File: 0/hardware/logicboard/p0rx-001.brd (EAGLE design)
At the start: 91 x 57 mm, 37 parts, among them IC1 LTC485N, IC2 LTC485N, IC3 LTC485N, IC4 LTC485N, IC5 74ALS05N, IC6 74ALS05N, J0 DC5V, J10 DIN5, J7 DIN5, J8 DIN5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

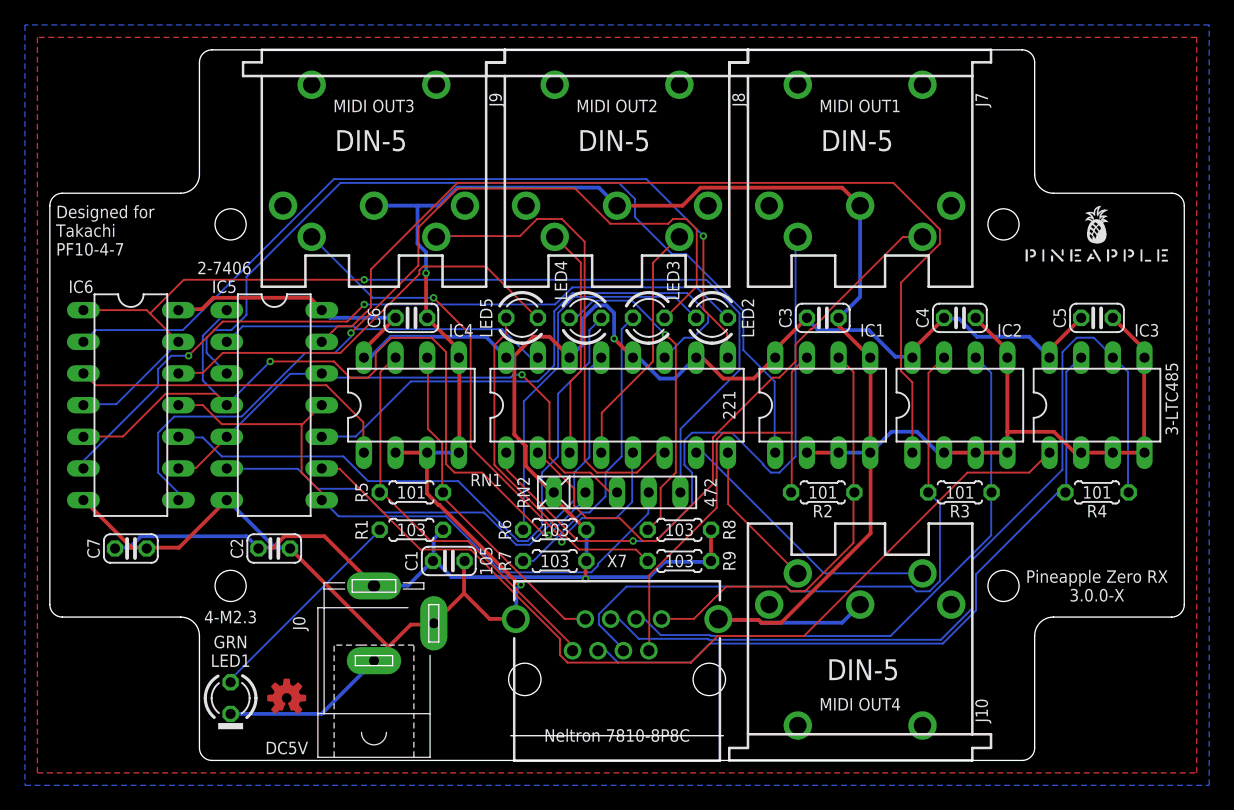
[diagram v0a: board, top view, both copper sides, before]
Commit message: Replaced Rs with RN.
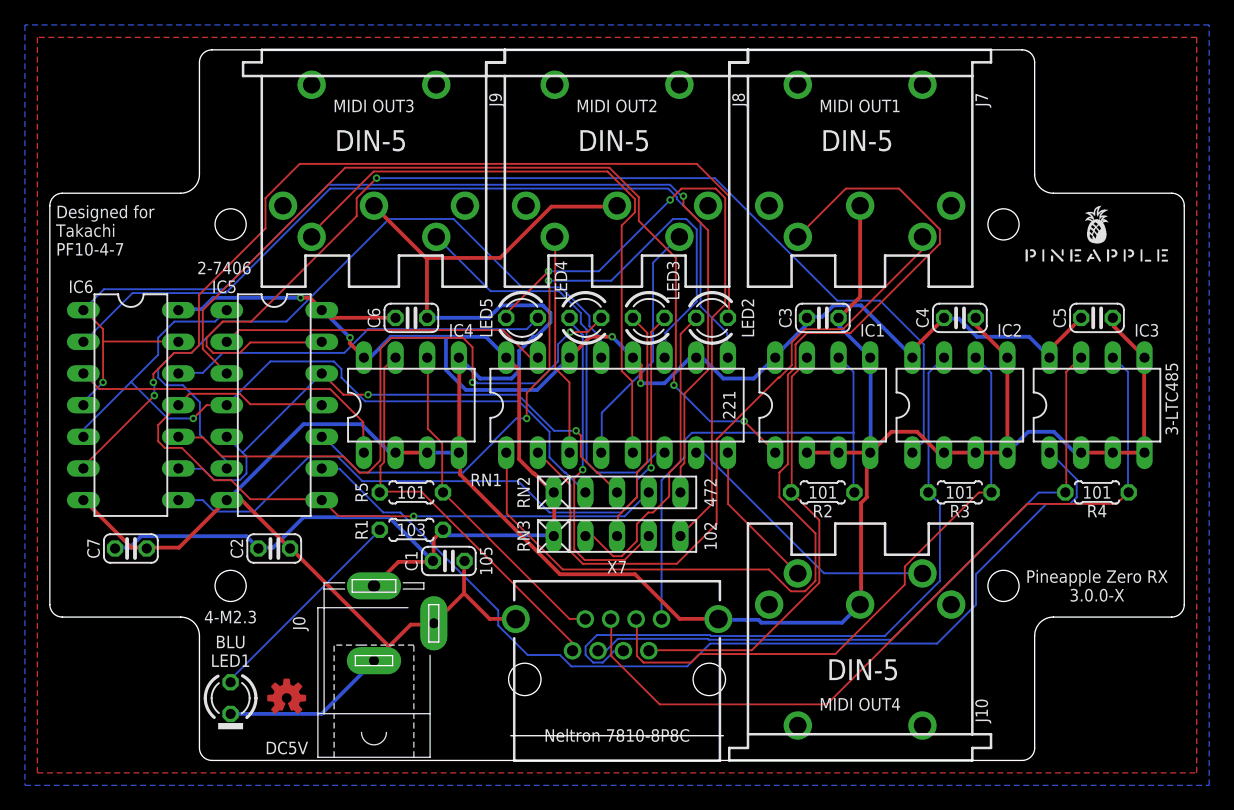
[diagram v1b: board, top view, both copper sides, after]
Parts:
- removed R6, R7, R8, R9: 102, rcl:0204/5
- added RN3: 1k, resistor-net:RN-5
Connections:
- net N$10: now also RN3.5; no longer R9.1
- net N$7: now also RN3.2; no longer R6.1
- net N$8: now also RN3.3; no longer R7.1
- net N$9: now also RN3.4; no longer R8.1
- net VCC: now also RN3.1; no longer R6.2, R7.2, R8.2, R9.2
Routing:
- net MO1SND: track 54.0 -> 83.8 mm, vias 1 -> 0
- net N$10: track 27.7 -> 51.0 mm, vias 0 -> 2
- net N$11: track 59.9 -> 77.8 mm
- net GND: track 255.8 -> 269.9 mm, vias 2 -> 0
- net MO2RTNRAW: track 44.2 -> 57.6 mm
- net MO3RTNRAW: track 44.4 -> 57.0 mm, vias 0 -> 2
- net N$12: track 69.2 -> 56.8 mm
- net RX2: track 77.8 -> 88.8 mm, vias 0 -> 1
- net VCC: track 178.8 -> 168.3 mm, vias 2 -> 4
- net N$1: track 84.3 -> 93.2 mm, vias 1 -> 2
- net RX3: track 72.6 -> 79.4 mm
- net RX3R: track 51.9 -> 58.5 mm, vias 0 -> 1
- net RX1R: track 69.0 -> 62.4 mm, vias 2 -> 1
- net RX1+: track 33.7 -> 40.3 mm
- net MO1RTN: track 47.7 -> 54.2 mm
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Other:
- board text added: "102"
- board text added: "BLU"
- board text removed: "GRN"

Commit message: Fixed wiring of 0.
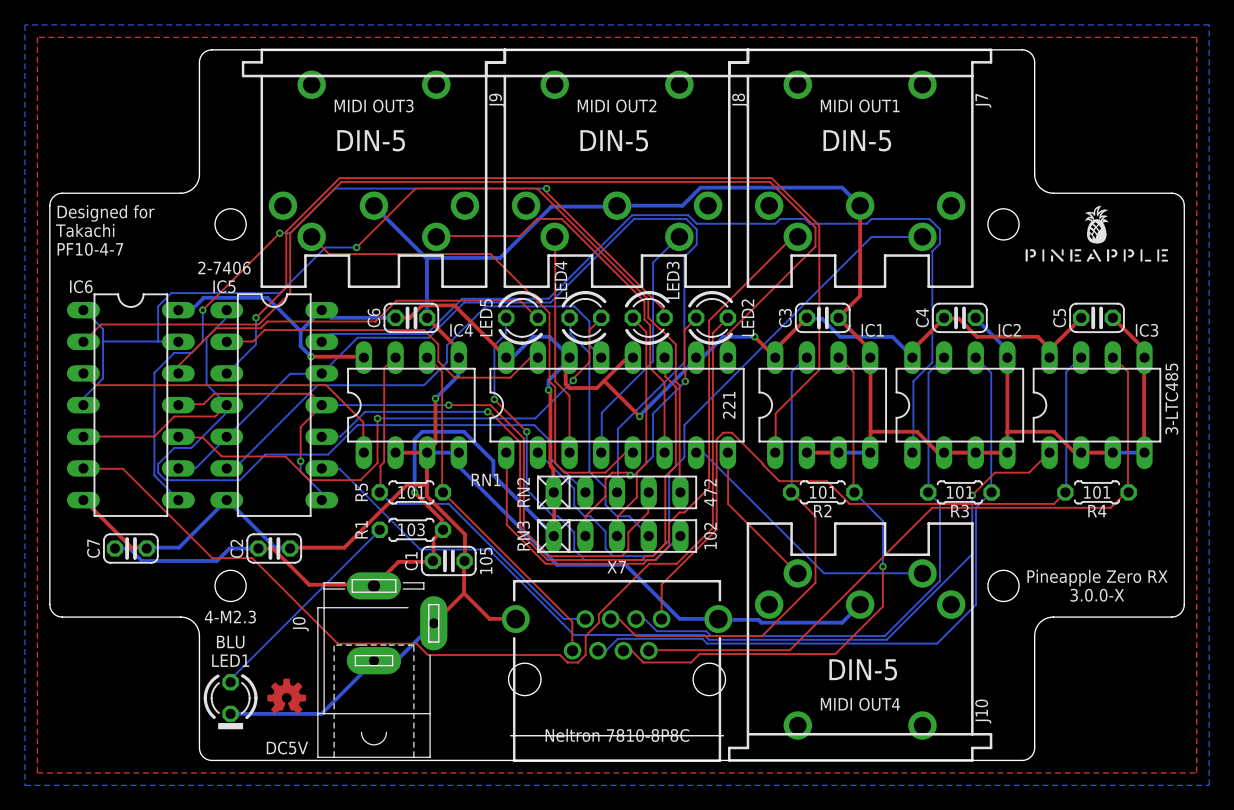
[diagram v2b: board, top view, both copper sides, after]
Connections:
- removed net N$3: IC4.6, R5.1, X7.7
- removed net N$5: IC4.7, R5.2, X7.8
- new net RX4+: IC4.6, R5.1, X7.8
- new net RX4-: IC4.7, R5.2, X7.7
- net RX1+: now also X7.4; no longer X7.1
- net RX1-: now also X7.5; no longer X7.2
- net RX2+: now also X7.6; no longer X7.3
- net RX2-: now also X7.3; no longer X7.4
- net RX3+: now also X7.2; no longer X7.5
- net RX3-: now also X7.1; no longer X7.6
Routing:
- net MO1SND: track 83.8 -> 50.3 mm
- net N$5: track 32.5 -> 0.00 mm
- net RX4-: track 0.00 -> 32.1 mm
- net RX4+: track 0.00 -> 28.4 mm
- net N$3: track 27.0 -> 0.00 mm
- net RX2R: track 47.3 -> 74.0 mm, vias 2 -> 0
- net N$10: track 51.0 -> 31.5 mm
- net MO2RTNRAW: track 57.6 -> 39.1 mm
- net GND: track 269.9 -> 254.3 mm, vias 0 -> 1
- net RX2: track 88.8 -> 73.7 mm, vias 1 -> 0
- net N$6: track 67.5 -> 81.7 mm
- net N$1: track 93.2 -> 81.3 mm, vias 2 -> 1
- net RX3+: track 64.5 -> 55.2 mm
- net MO3SND: track 50.3 -> 41.0 mm
- net RX2-: track 53.9 -> 45.6 mm
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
